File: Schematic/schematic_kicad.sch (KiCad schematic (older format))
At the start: 244 parts

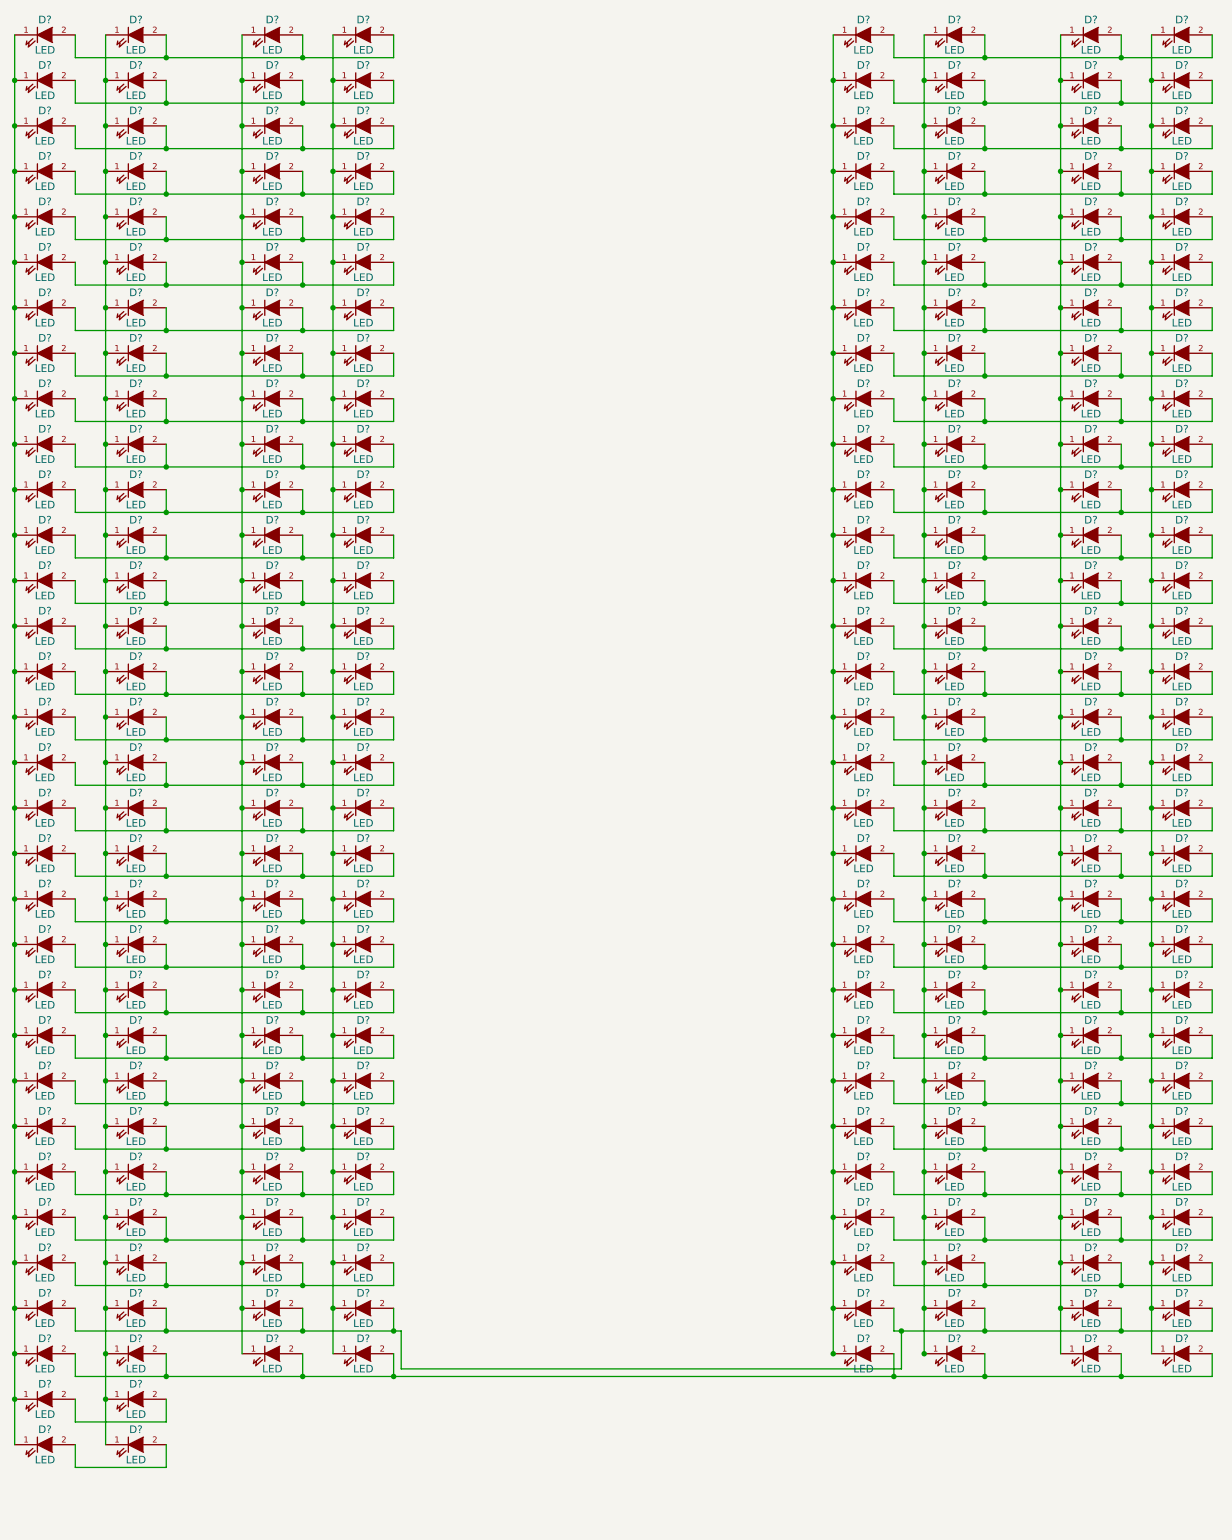
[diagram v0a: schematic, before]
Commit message: Added library and schematic changes
Annotated LEDs and added some of the shift registers needed for the
design. Found a library for msp430 schematics on 43oh forum.
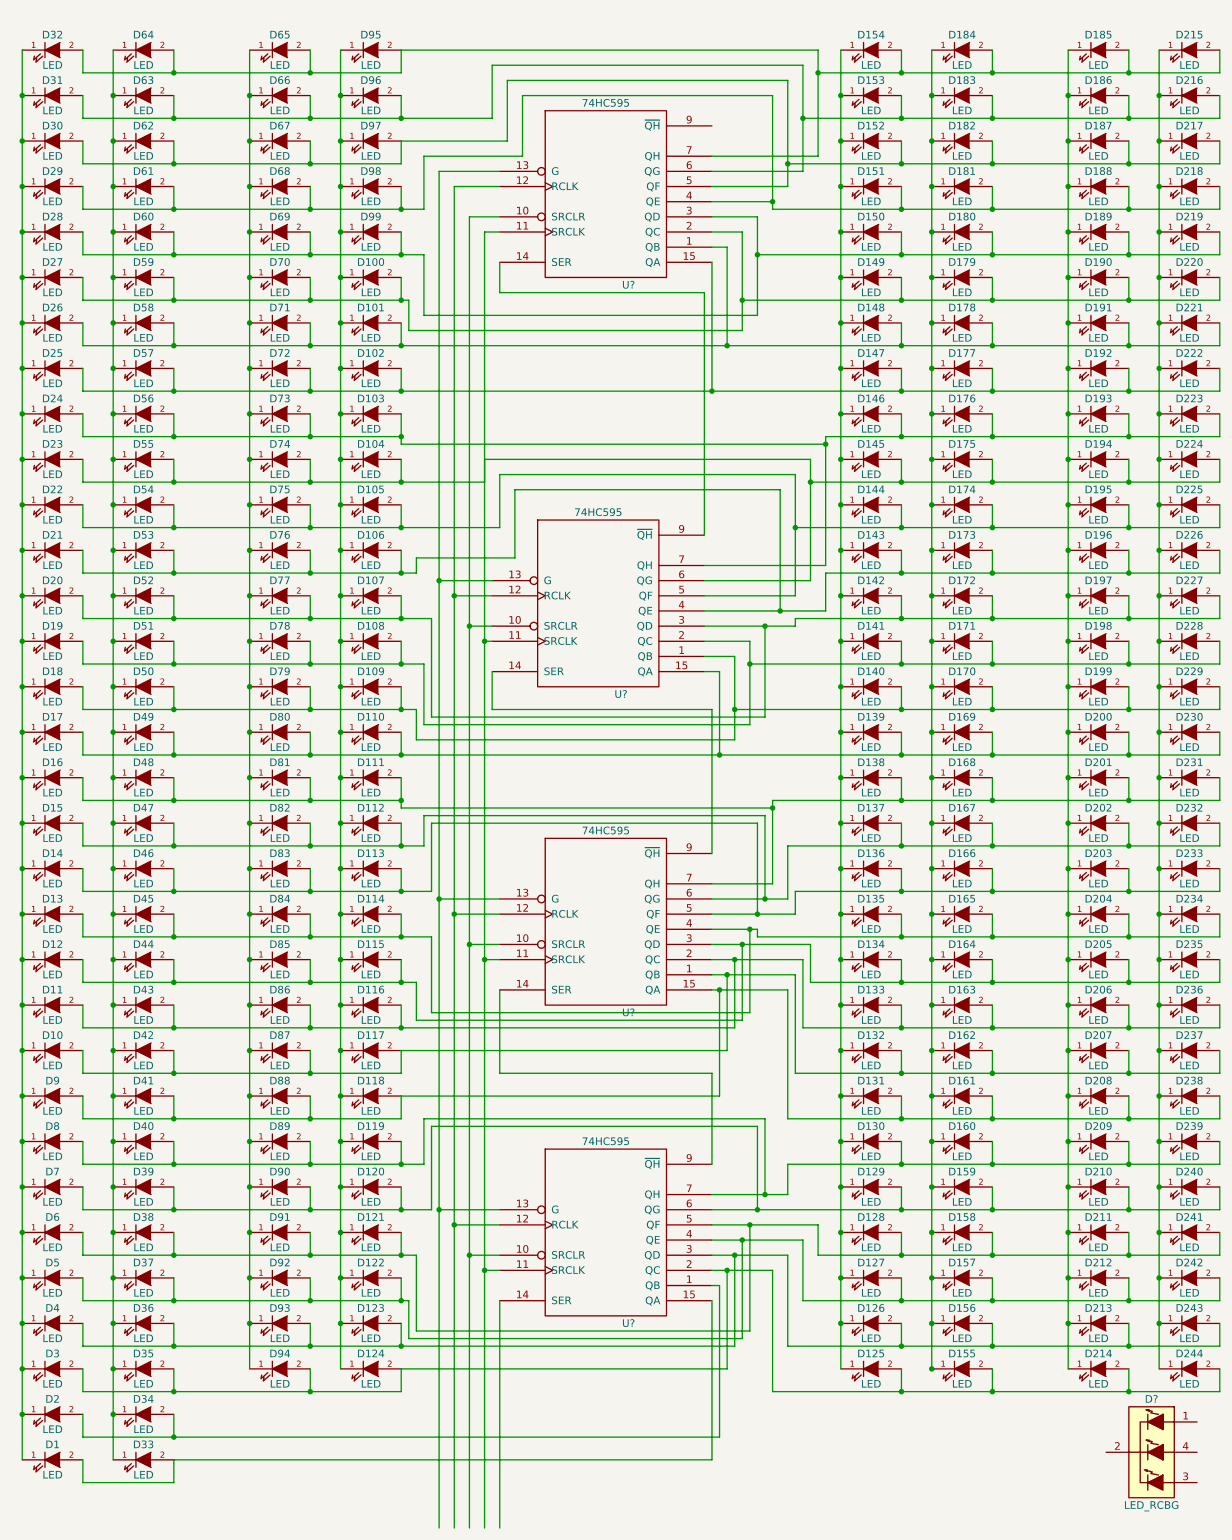
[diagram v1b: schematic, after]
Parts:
- added D?: LED_RCBG, symbol LED_RCBG
- added U? (x4): 74HC595, symbol 74HC595
- gave numbers to parts that had none: 244
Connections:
- net at D32.2 (A), D64.2 (A), D65.2 (A)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: now also D154.2 (A), D184.2 (A), D185.2 (A), D215.2 (A), U?.7 (QH)
- net at D31.2 (A), D63.2 (A), D66.2 (A)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: now also D153.2 (A), D183.2 (A), D186.2 (A), D216.2 (A), U?.6 (QG)
- net at D30.2 (A), D62.2 (A), D67.2 (A)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: now also D152.2 (A), D182.2 (A), D187.2 (A), D217.2 (A), U?.5 (QF)
- net at D29.2 (A), D61.2 (A), D68.2 (A)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: now also D151.2 (A), D181.2 (A), D188.2 (A), D218.2 (A), U?.4 (QE)
- net at D28.2 (A), D60.2 (A), D69.2 (A)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: now also D150.2 (A), D180.2 (A), D189.2 (A), D219.2 (A), U?.3 (QD)
- net at D100.2 (A), D27.2 (A), D59.2 (A)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: now also D149.2 (A), D179.2 (A), D190.2 (A), D220.2 (A), U?.2 (QC)
- net at D101.2 (A), D26.2 (A), D58.2 (A)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: now also D148.2 (A), D178.2 (A), D191.2 (A), D221.2 (A), U?.1 (QB)
- net at D102.2 (A), D25.2 (A), D57.2 (A)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: now also D147.2 (A), D177.2 (A), D192.2 (A), D222.2 (A), U?.15 (QA)
- net at D103.2 (A), D24.2 (A), D56.2 (A)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: now also D146.2 (A), D176.2 (A), D193.2 (A), D223.2 (A), U?.7 (QH)
- net at D104.2 (A), D23.2 (A), D55.2 (A)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: now also D145.2 (A), D175.2 (A), D194.2 (A), D224.2 (A), U?.11 (SRCLK), U?.11 (SRCLK), U?.11 (SRCLK), U?.11 (SRCLK), U?.6 (QG)
- net at D105.2 (A), D22.2 (A), D54.2 (A)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: now also D144.2 (A), D174.2 (A), D195.2 (A), D225.2 (A), U?.5 (QF)
- net at D106.2 (A), D21.2 (A), D53.2 (A)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: now also D143.2 (A), D173.2 (A), D196.2 (A), D226.2 (A), U?.4 (QE)
- net at D107.2 (A), D20.2 (A), D52.2 (A)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: now also D142.2 (A), D172.2 (A), D197.2 (A), D227.2 (A), U?.3 (QD)
- net at D108.2 (A), D19.2 (A), D51.2 (A)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: now also D141.2 (A), D171.2 (A), D198.2 (A), D228.2 (A), U?.2 (QC)
- net at D109.2 (A), D18.2 (A), D50.2 (A)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: now also D140.2 (A), D170.2 (A), D199.2 (A), D229.2 (A), U?.1 (QB)
- net at D110.2 (A), D17.2 (A), D49.2 (A)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: now also D139.2 (A), D169.2 (A), D200.2 (A), D230.2 (A), U?.15 (QA)
- net at D111.2 (A), D16.2 (A), D48.2 (A)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: now also D138.2 (A), D168.2 (A), D201.2 (A), D231.2 (A), U?.7 (QH)
- net at D112.2 (A), D15.2 (A), D47.2 (A)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: now also D137.2 (A), D167.2 (A), D202.2 (A), D232.2 (A), U?.6 (QG)
- net at D113.2 (A), D14.2 (A), D46.2 (A)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: now also D136.2 (A), D166.2 (A), D203.2 (A), D233.2 (A), U?.5 (QF)
- net at D114.2 (A), D13.2 (A), D45.2 (A)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: now also D135.2 (A), D165.2 (A), D204.2 (A), D234.2 (A), U?.4 (QE)
- net at D115.2 (A), D12.2 (A), D44.2 (A)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: now also D134.2 (A), D164.2 (A), D205.2 (A), D235.2 (A), U?.3 (QD)
- net at D11.2 (A), D116.2 (A), D43.2 (A)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: now also D133.2 (A), D163.2 (A), D206.2 (A), D236.2 (A), U?.2 (QC)
- net at D10.2 (A), D117.2 (A), D42.2 (A)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: now also D132.2 (A), D162.2 (A), D207.2 (A), D237.2 (A), U?.1 (QB)
- net at D118.2 (A), D41.2 (A), D88.2 (A)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: now also D131.2 (A), D161.2 (A), D208.2 (A), D238.2 (A), U?.15 (QA)
- net at D119.2 (A), D40.2 (A), D8.2 (A)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: now also D130.2 (A), D160.2 (A), D209.2 (A), D239.2 (A), U?.7 (QH)
- net at D120.2 (A), D39.2 (A), D7.2 (A)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: now also D129.2 (A), D159.2 (A), D210.2 (A), D240.2 (A), U?.6 (QG)
- net at D121.2 (A), D38.2 (A), D6.2 (A)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: now also D128.2 (A), D158.2 (A), D211.2 (A), D241.2 (A), U?.5 (QF)
- net at D122.2 (A), D37.2 (A), D5.2 (A)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: now also D127.2 (A), D157.2 (A), D212.2 (A), D242.2 (A), U?.4 (QE)
- net at D123.2 (A), D126.2 (A), D156.2 (A)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: now also U?.3 (QD)
- net at D124.2 (A), D125.2 (A), D155.2 (A)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: now also U?.2 (QC)
- net at D2.2 (A), D34.2 (A): now also U?.1 (QB)
- net at D1.2 (A), D33.2 (A): now also U?.15 (QA)
- new net: U?.10 (SRCLR), U?.10 (SRCLR), U?.10 (SRCLR), U?.10 (SRCLR)
- new net: U?.12 (RCLK), U?.12 (RCLK), U?.12 (RCLK), U?.12 (RCLK)
- new net: U?.13 (G), U?.13 (G), U?.13 (G), U?.13 (G)
- new net: U?.14 (SER), U?.9 (~QH) (x3)
- new net GND: U?.8 (GND), U?.8 (GND), U?.8 (GND), U?.8 (GND)
- new net VCC: U?.16 (VCC), U?.16 (VCC), U?.16 (VCC), U?.16 (VCC)
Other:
- moved on the sheet: D1, D10, D100, D101, D102, D103, D104, D105, D106, D107, D108, D109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

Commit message: Rearranged LEDs
LEDs were moved to reflect changes in plans for the physical board
layout. This change will make it easier to wire it to the shift
registers.
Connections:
- wire segments 466 -> 350
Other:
- moved on the sheet: D125, D126, D127, D128, D129, D130, D131, D132, D133, D134, D135, D136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

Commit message: Added 7 segment displays, Shift Register changes
Changed the wiring to the shift registers to reflect designs made on the
prototype to reduce wiring complexity. Added the plan for the seven
segment displays and their shift registers. Prototype has all LEDs and
connections to shift registers currently.
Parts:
- removed U? (x2): 74HC595, symbol 74HC595
- added AFF? (x5): 7SEGMENTS, symbol 7SEGMENTS
- added R? (x19): R, symbol R
- added U? (x5): 74HC595, symbol 74HC595
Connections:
- wire segments 350 -> 587
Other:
- moved on the sheet: D?, U?

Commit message: Added resistor values and buttons
The button were added to match the physical layout general design,
however the shift registers connected to them were not yet added.
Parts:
- removed D?: LED_RCBG, symbol LED_RCBG
- added D?: LED_RABG, symbol LED_RABG
- added R? (x5): 470, symbol R
- added SW? (x23): SW_PUSH, symbol SW_PUSH
- R? (x7): value R -> 470
- R? (x12): value R -> 200
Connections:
- net at D1.1 (K), D10.1 (K), D11.1 (K)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: now also R?.1; no longer R?.1
- net at D33.1 (K), D34.1 (K), D35.1 (K)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: now also R?.1; no longer R?.1
- net at D65.1 (K), D66.1 (K), D67.1 (K)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: now also R?.1; no longer R?.1
- net at D100.1 (K), D101.1 (K), D102.1 (K)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: now also R?.1; no longer R?.1
- net at AFF?.3 (C.A.), AFF?.8 (C.A.): now also R?.1; no longer U?.3 (QD)
- net at AFF?.3 (C.A.), AFF?.8 (C.A.): now also R?.1; no longer U?.4 (QE)
- net at AFF?.3 (C.A.), AFF?.8 (C.A.): now also R?.1; no longer U?.5 (QF)
- net at AFF?.3 (C.A.), AFF?.8 (C.A.): now also R?.1; no longer U?.6 (QG)
- net at AFF?.3 (C.A.), AFF?.8 (C.A.): now also R?.1; no longer U?.7 (QH)
- net at D125.1 (K), D126.1 (K), D127.1 (K)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: now also R?.1; no longer R?.1
- net at R?.1: now also D?.1 (RED_CATHODE)
- net at D155.1 (K), D156.1 (K), D157.1 (K)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: now also R?.1; no longer R?.1
- net at D185.1 (K), D186.1 (K), D187.1 (K)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: now also R?.1; no longer R?.1
- net at D215.1 (K), D216.1 (K), D217.1 (K)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: now also R?.1; no longer R?.1
- net at R?.1: now also D?.4 (GREEN_CATHODE)
- net at R?.1: now also D?.3 (BLUE_CATHODE)
- new net: R?.2, U?.3 (QD)
- new net: R?.2, U?.4 (QE)
- new net: R?.2, U?.5 (QF)
- new net: R?.2, U?.6 (QG)
- new net: R?.2, U?.7 (QH)
- new net +3V3: D?.2 (COMMON_ANODE)
